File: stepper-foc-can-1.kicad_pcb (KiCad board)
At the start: 4 copper layers, 42 x 42 mm, 84 parts, among them J1 TC2030, J2 Conn_01x02, J3 Conn_01x04_Pin, J4 Conn_01x02, J5 Conn_01x02, M1 Stepper_Motor_bipolar, SW1 SW_Push, SW2 SW_Push, SW3 SW_Push, U1 STM32G474RBTx, U2 MX25947, U3 TPS62933, U4 TCAN3413, U5 AS5047P, U6 DRV8874, U7 INA241A3IDDF, U8 DRV8874, U9 INA241A3IDDF, Y1 Crystal_GND24

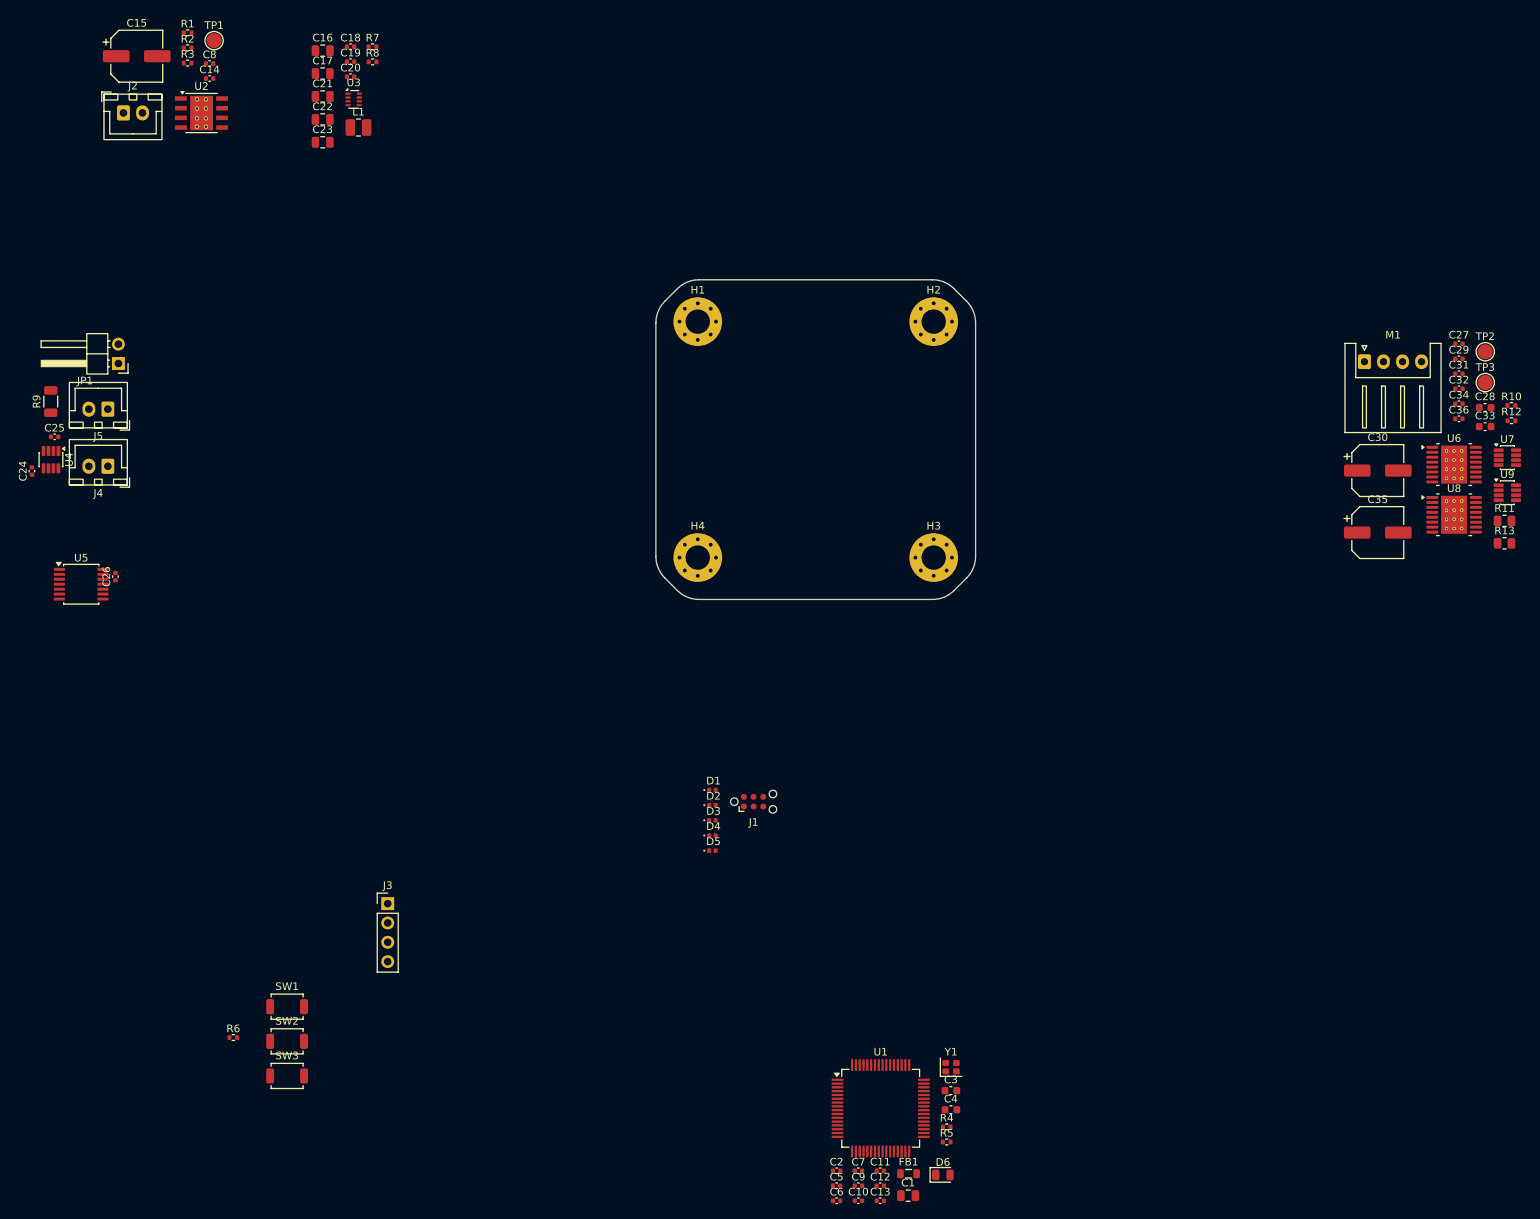
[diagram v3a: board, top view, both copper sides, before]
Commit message: pcb: add efuse layout
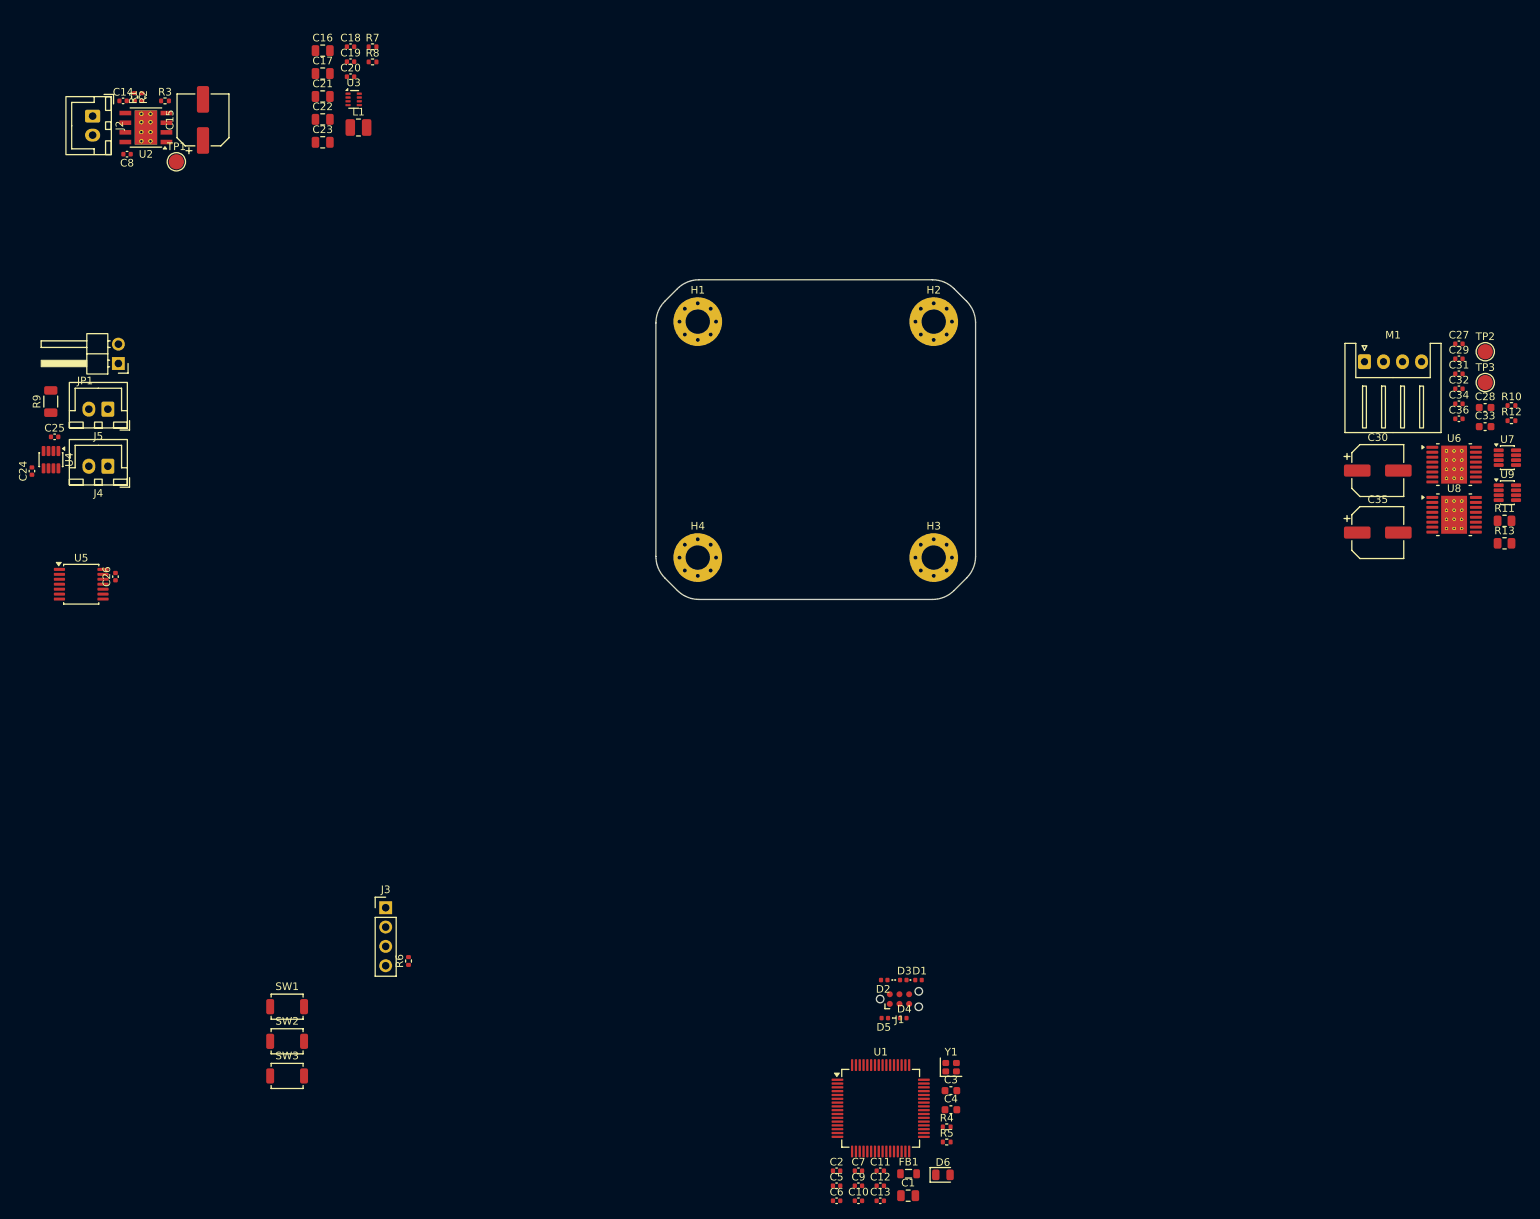
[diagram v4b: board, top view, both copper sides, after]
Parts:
- moved D1 36.8 mm to (157.5, 152.0)
- moved D4 34.7 mm to (155.5, 157.0)
- moved D3 32.7 mm to (155.5, 152.0)
- moved J1 32.2 mm to (155.0, 154.5)
- moved D2 32.2 mm to (153.0, 152.0), turned to 180 degrees
- moved D5 31.6 mm to (153.1, 157.0), turned to 180 degrees
- moved R6 25.1 mm to (90.5, 149.5), turned to 90 degrees
- moved TP1 16.7 mm to (60.0, 44.5)
- moved C8 16.1 mm to (53.5, 43.5), turned to 180 degrees
- moved C15 12.1 mm to (63.5, 39.0), turned to 90 degrees
- moved C14 11.7 mm to (53.0, 36.5)
- moved R1 10.4 mm to (55.5, 36.0), turned to 90 degrees
- moved R2 9.51 mm to (54.5, 36.0), turned to -90 degrees
- moved U2 7.54 mm to (56.0, 40.0), turned to 180 degrees
- moved R3 5.79 mm to (58.5, 36.5)
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
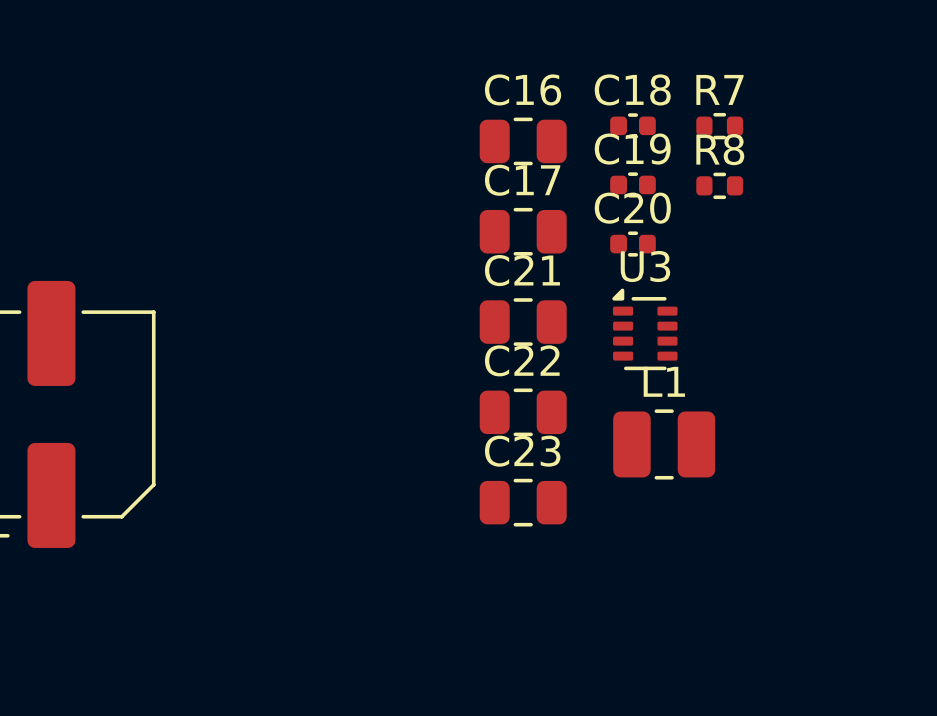
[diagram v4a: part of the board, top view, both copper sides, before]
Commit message: pcb: add smps layout
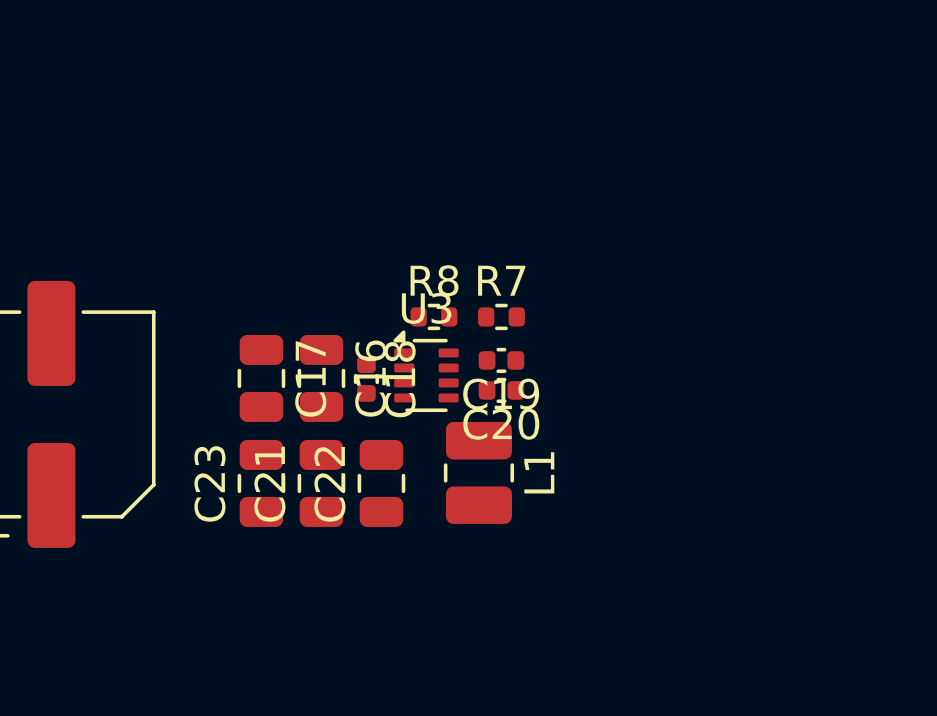
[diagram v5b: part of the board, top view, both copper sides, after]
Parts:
- moved C18 12.3 mm to (74.0, 37.8), turned to -90 degrees
- moved R8 10.5 mm to (76.2, 35.8)
- moved C16 10.4 mm to (72.5, 37.8), turned to -90 degrees
- moved C17 10.0 mm to (70.5, 37.8), turned to -90 degrees
- moved R7 9.66 mm to (78.5, 35.8)
- moved C23 8.75 mm to (70.5, 41.3), turned to 90 degrees
- moved C21 8.61 mm to (72.5, 41.3), turned to 90 degrees
- moved U3 7.43 mm to (76.0, 37.7)
- moved C19 7.31 mm to (78.5, 37.2), turned to 180 degrees
- moved C20 6.56 mm to (78.5, 38.2), turned to 180 degrees
- moved L1 6.25 mm to (77.8, 41.0), turned to -90 degrees
- moved C22 5.29 mm to (74.5, 41.3), turned to 90 degrees

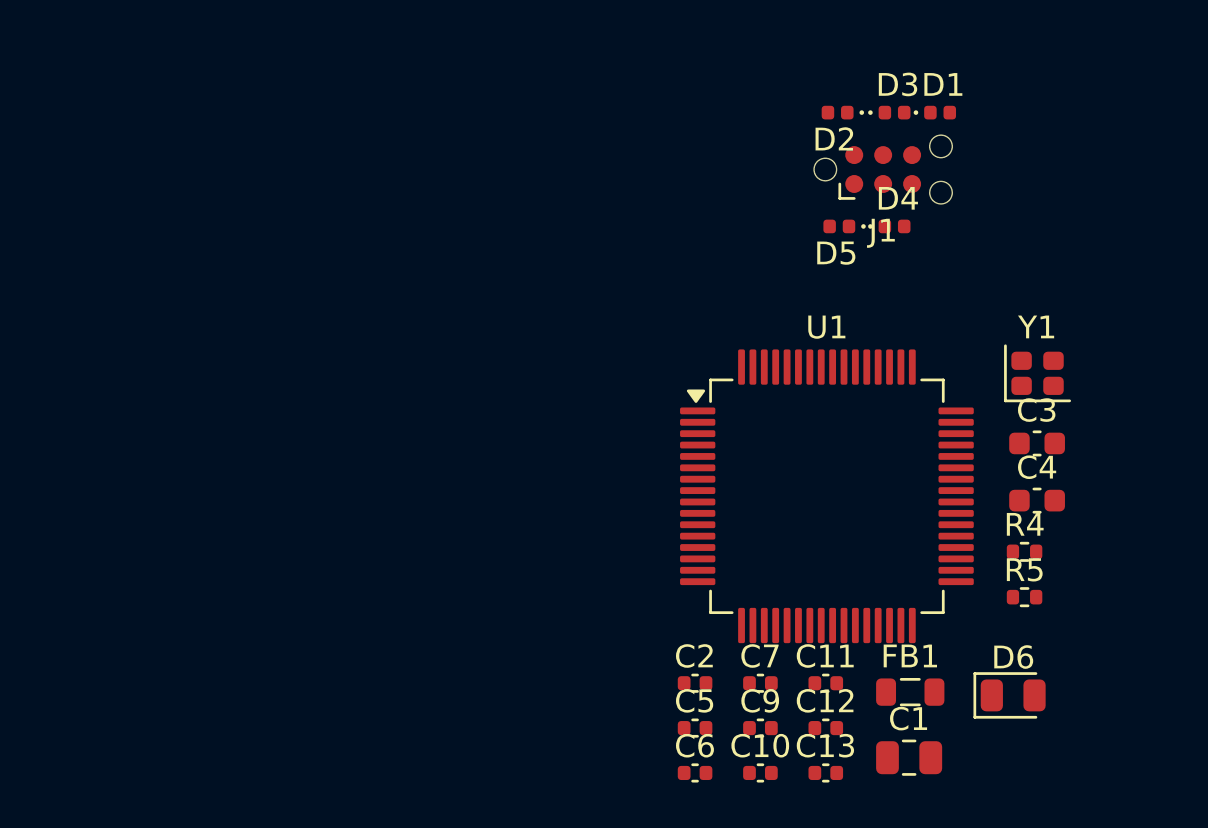
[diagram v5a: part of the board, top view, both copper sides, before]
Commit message: pcb: add stm32 layout
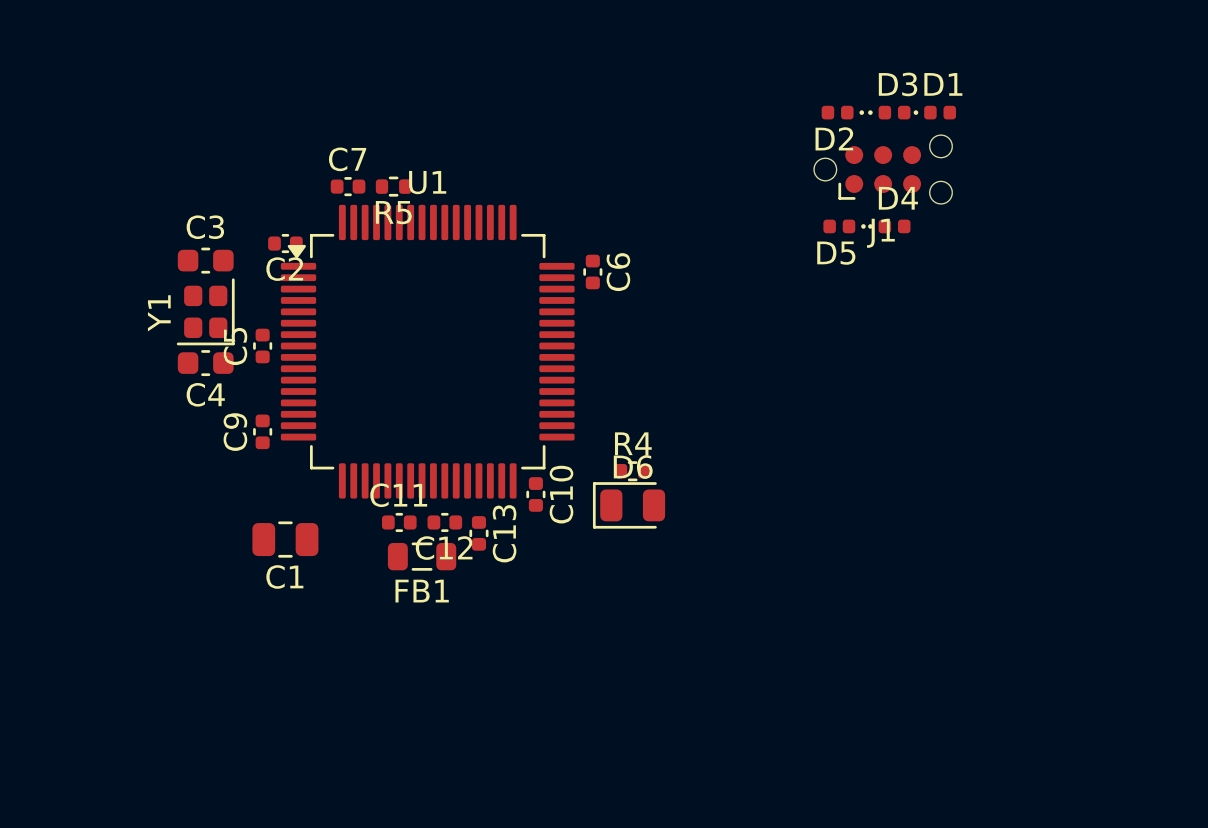
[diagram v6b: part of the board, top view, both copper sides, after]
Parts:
- moved C3 37.4 mm to (125.2, 158.5)
- moved C4 37.0 mm to (125.2, 163.0), turned to 180 degrees
- moved Y1 36.6 mm to (125.2, 160.8), turned to 90 degrees
- moved R5 33.1 mm to (133.5, 155.2), turned to 180 degrees
- moved C1 29.0 mm to (128.8, 170.8), turned to 180 degrees
- moved C7 28.3 mm to (131.5, 155.2)
- moved C2 26.4 mm to (128.8, 157.8), turned to 180 degrees
- moved C9 25.4 mm to (127.8, 166.0), turned to 90 degrees
- moved C5 25.3 mm to (127.8, 162.2), turned to 90 degrees
- moved C6 22.5 mm to (142.2, 159.0), turned to -90 degrees
- moved FB1 22.3 mm to (134.8, 171.5), turned to 180 degrees
- moved C11 20.0 mm to (133.8, 170.0)
- moved C12 19.0 mm to (135.8, 170.0), turned to 180 degrees
- moved D6 18.7 mm to (144.0, 169.2)
- moved U1 18.6 mm to (135.0, 162.5)
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
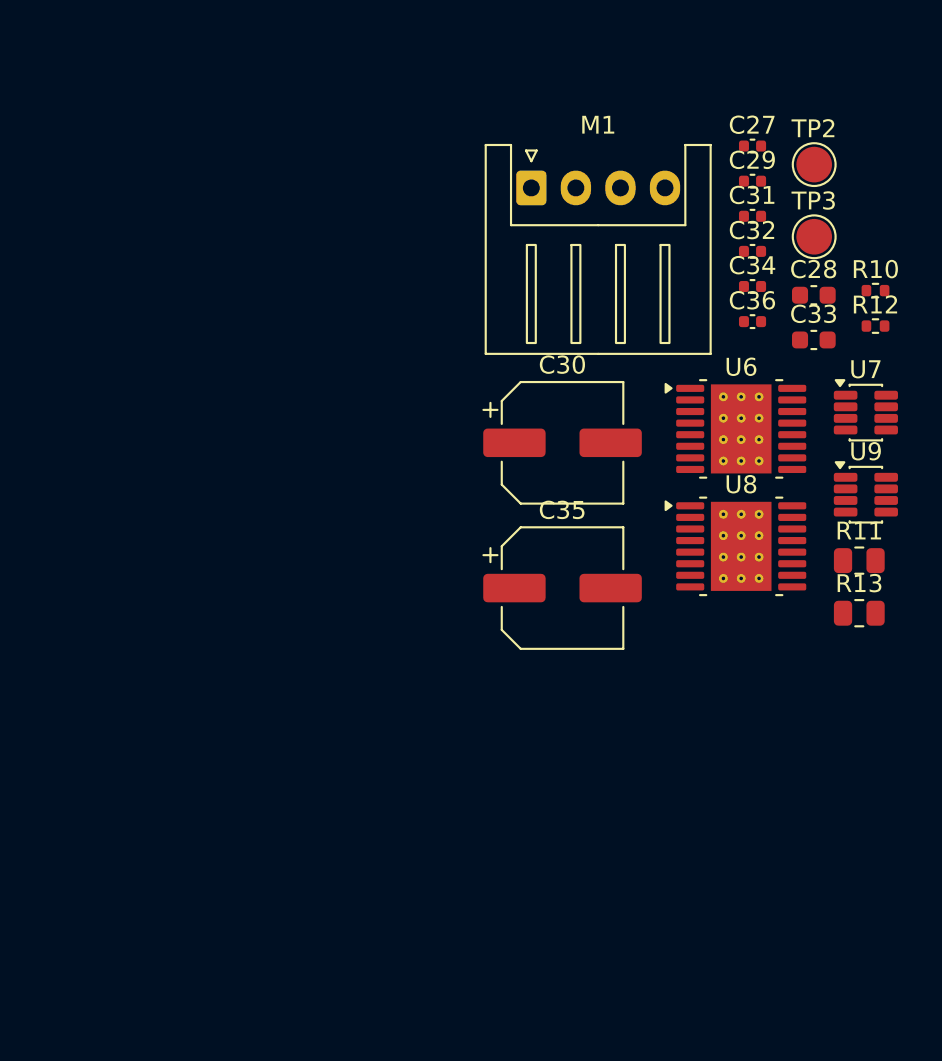
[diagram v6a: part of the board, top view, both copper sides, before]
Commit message: pcb: add stepper drvs layout
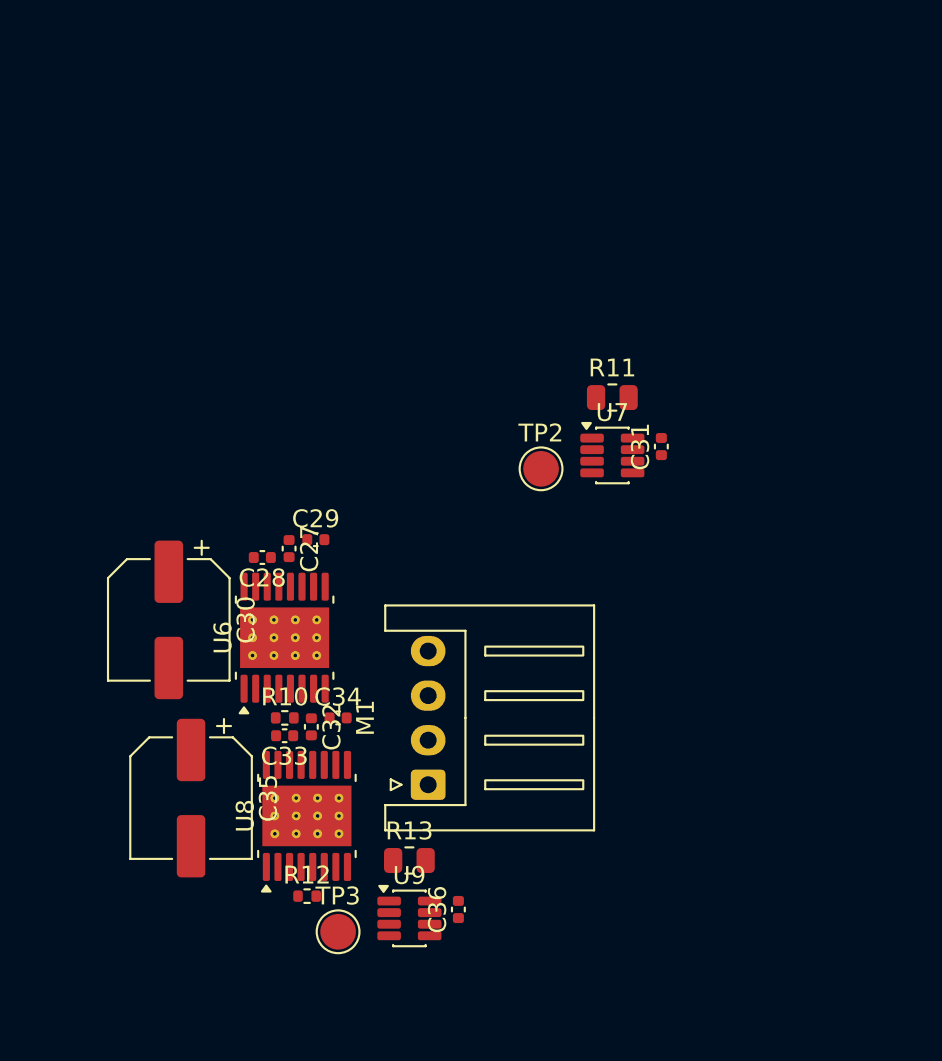
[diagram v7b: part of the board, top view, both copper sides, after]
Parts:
- C28, C33: footprint Capacitor_SMD:C_0603_1608Metric -> Capacitor_SMD:C_0402_1005Metric
- moved TP3 47.3 mm to (205.2, 112.5)
- moved R12 45.2 mm to (203.5, 110.5)
- moved R10 40.9 mm to (202.3, 100.5)
- moved C33 37.1 mm to (202.2, 101.5), turned to 180 degrees
- moved C36 36.9 mm to (212.0, 111.2), turned to 90 degrees
- moved C32 36.4 mm to (203.8, 101.0), turned to -90 degrees
- moved U9 34.9 mm to (209.2, 111.8)
- moved C27 34.4 mm to (202.5, 91.0), turned to -90 degrees
- moved C28 34.3 mm to (201.0, 91.5), turned to 180 degrees
- moved M1 34.0 mm to (210.3, 104.2), turned to 90 degrees
- moved C34 33.6 mm to (205.2, 100.5)
- moved C29 31.7 mm to (204.0, 90.5)
- moved R13 28.8 mm to (209.2, 108.5)
- moved U8 28.7 mm to (203.5, 106.0), turned to 90 degrees
- moved U6 28.2 mm to (202.2, 96.0), turned to 90 degrees
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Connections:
- U6 pad 17: (no net) -> GND
- U8 pad 17: (no net) -> GND
